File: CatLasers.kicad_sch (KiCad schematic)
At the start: 6 parts, among them J2 Programmer, J4 IR Emitter, J6 Conn_01x04, U2 ESP32-WROOM-32E_(4MB_HIGH_TEM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

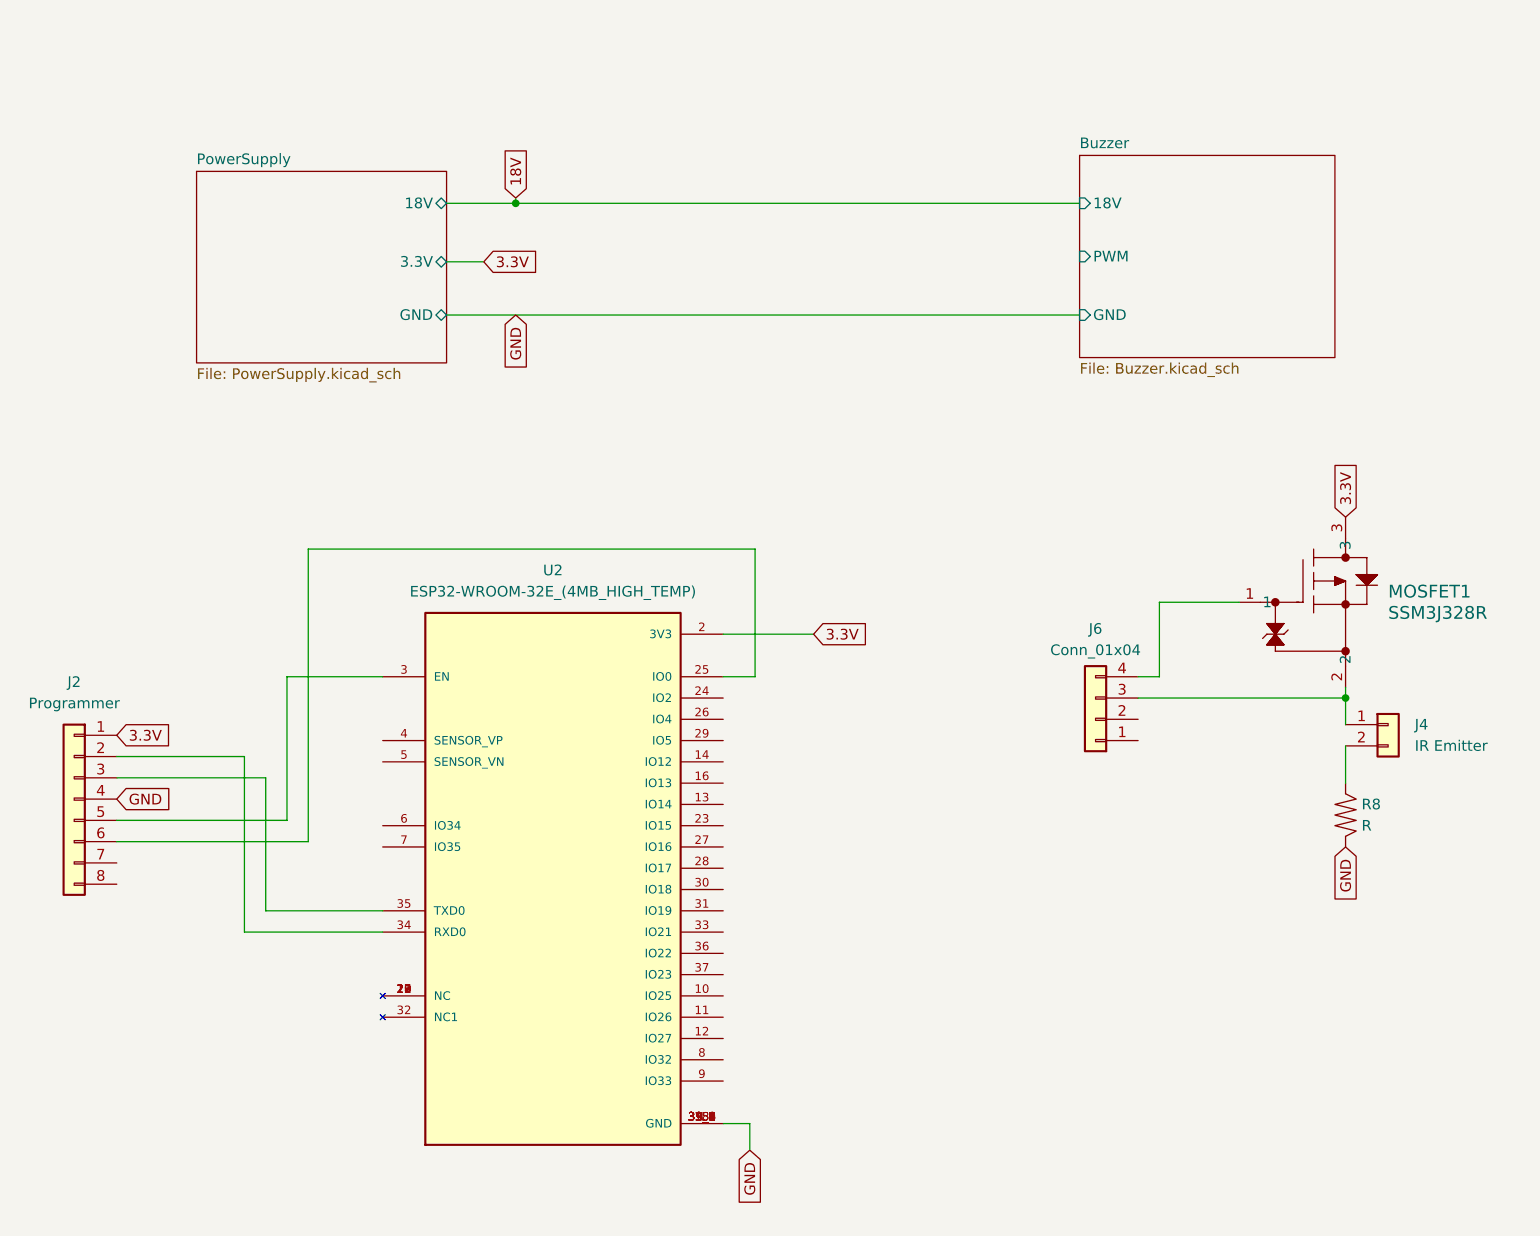
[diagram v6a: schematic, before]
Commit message: Wired MCU jumpers
All MCU pins are sent directly to jumpers. This will double as testpoints and a way for me to easily rewire the test board.
Footprints also assigned
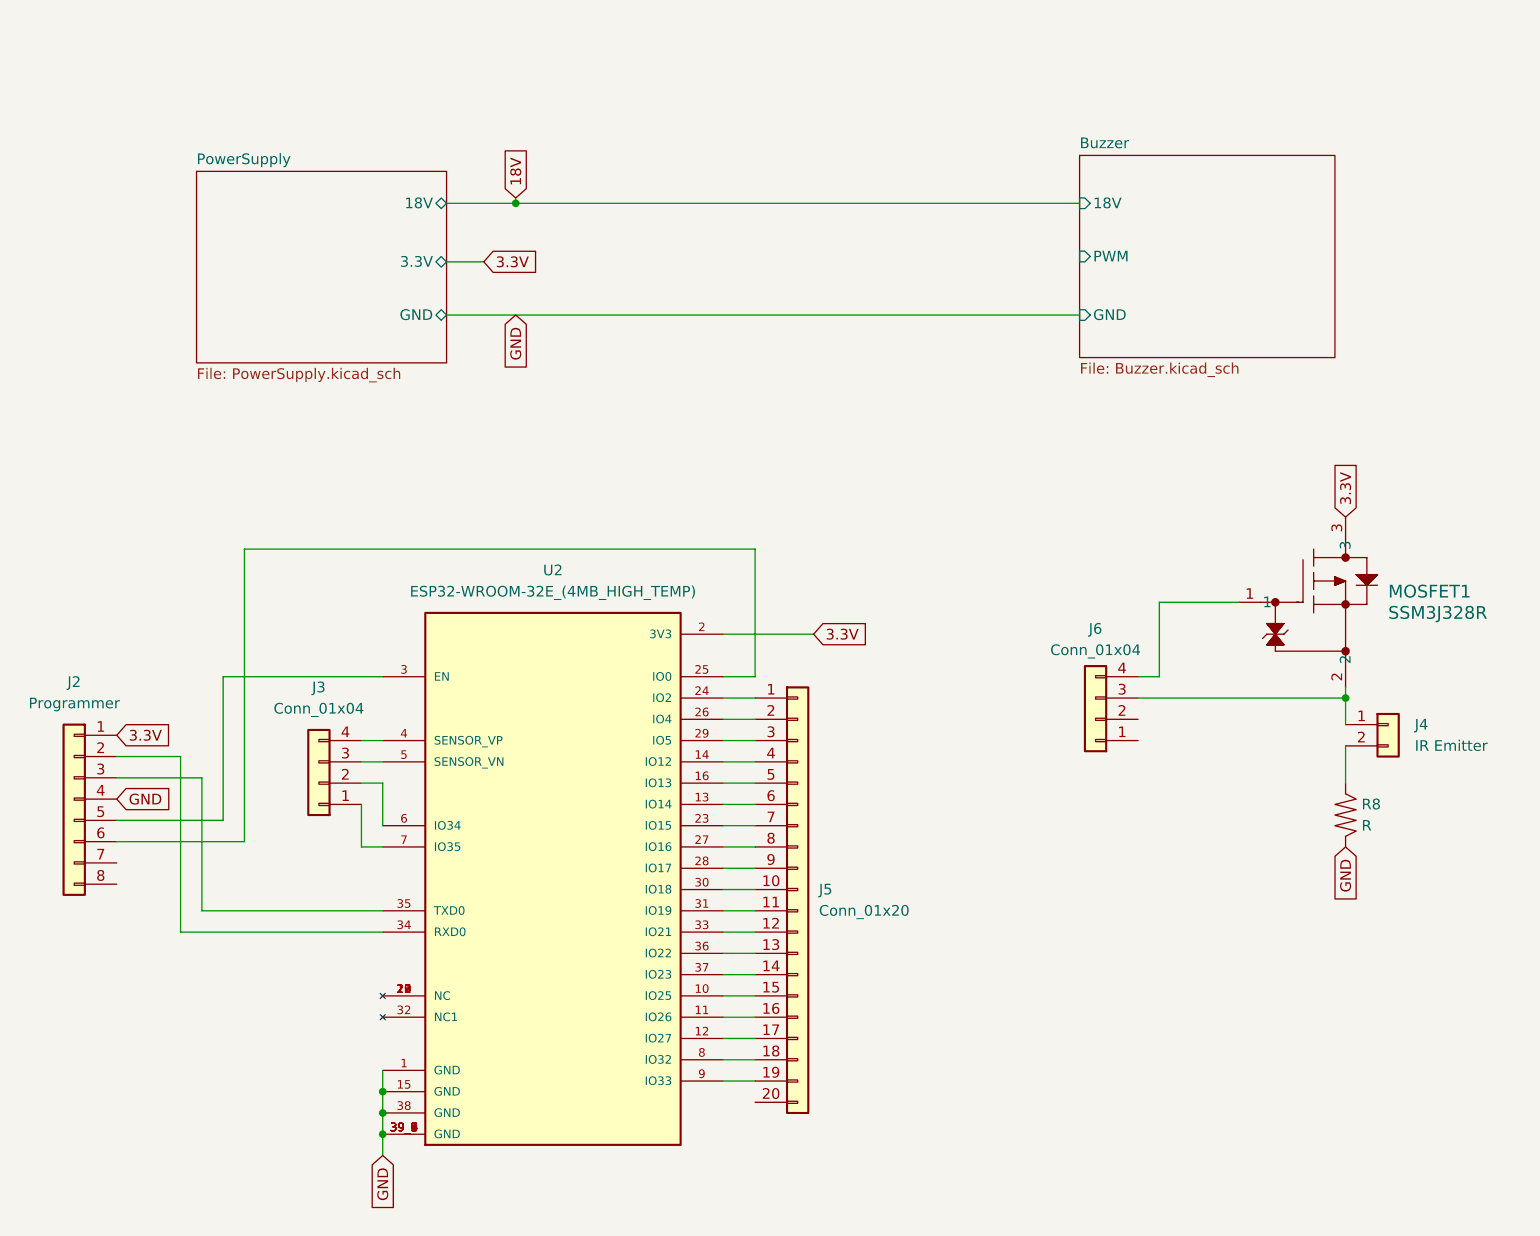
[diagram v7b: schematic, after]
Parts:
- added J3: Conn_01x04, Connector_PinHeader_2.54mm:PinHeader_1x04_P2.54mm_Vertical, symbol Connector_Generic:Conn_01x04
- added J5: Conn_01x20, Connector_PinHeader_2.54mm:PinHeader_1x20_P2.54mm_Vertical, symbol Connector_Generic:Conn_01x20
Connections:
- net at U2.10 (IO25): now also J5.15 (Pin_15)
- net at U2.11 (IO26): now also J5.16 (Pin_16)
- net at U2.12 (IO27): now also J5.17 (Pin_17)
- net at U2.13 (IO14): now also J5.6 (Pin_6)
- net at U2.14 (IO12): now also J5.4 (Pin_4)
- net at U2.16 (IO13): now also J5.5 (Pin_5)
- net at U2.23 (IO15): now also J5.7 (Pin_7)
- net at U2.24 (IO2): now also J5.1 (Pin_1)
- net at U2.26 (IO4): now also J5.2 (Pin_2)
- net at U2.27 (IO16): now also J5.8 (Pin_8)
- net at U2.28 (IO17): now also J5.9 (Pin_9)
- net at U2.29 (IO5): now also J5.3 (Pin_3)
- net at U2.30 (IO18): now also J5.10 (Pin_10)
- net at U2.31 (IO19): now also J5.11 (Pin_11)
- net at U2.33 (IO21): now also J5.12 (Pin_12)
- net at U2.36 (IO22): now also J5.13 (Pin_13)
- net at U2.37 (IO23): now also J5.14 (Pin_14)
- net at U2.4 (SENSOR_VP): now also J3.4 (Pin_4)
- net at U2.5 (SENSOR_VN): now also J3.3 (Pin_3)
- net at U2.6 (IO34): now also J3.2 (Pin_2)
- net at U2.7 (IO35): now also J3.1 (Pin_1)
- net at U2.8 (IO32): now also J5.18 (Pin_18)
- net at U2.9 (IO33): now also J5.19 (Pin_19)
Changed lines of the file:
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@@
   (junction (at 179.705 101.6) (diameter 0) (color 0 0 0 0)
   )
-  (wire (pts (xy 109.22 83.82) (xy 55.88 83.82))
-    (stroke (width 0) (type default))
-  )
-  (wire (pts (xy 50.8 111.125) (xy 33.02 111.125))
-    (stroke (width 0) (type default))
-  )
-  (wire (pts (xy 64.77 127) (xy 50.8 127))
+  (junction (at 64.77 153.67) (diameter 0) (color 0 0 0 0)
+  )
+  (junction (at 64.77 151.13) (diameter 0) (color 0 0 0 0)
+  )
+  (junction (at 64.77 148.59) (diameter 0) (color 0 0 0 0)
+  )
+  (wire (pts (xy 109.22 137.16) (xy 105.41 137.16))
+    (stroke (width 0) (type default))
+  )
+  (wire (pts (xy 109.22 83.82) (xy 48.26 83.82))
+    (stroke (width 0) (type default))
+  )
+  (wire (pts (xy 109.22 83.82) (xy 109.22 99.06))
+    (stroke (width 0) (type default))
+  )
+  (wire (pts (xy 109.22 144.78) (xy 105.41 144.78))
+    (stroke (width 0) (type default))
+  )
+  (wire (pts (xy 43.18 111.125) (xy 33.02 111.125))
+    (stroke (width 0) (type default))
+  )
+  (wire (pts (xy 64.77 127) (xy 43.18 127))
     (stroke (width 0) (type default))
   )
@@
     (stroke (width 0) (type default))
   )
-  (wire (pts (xy 50.8 127) (xy 50.8 111.125))
+  (wire (pts (xy 43.18 127) (xy 43.18 111.125))
     (stroke (width 0) (type default))
   )
@@
     (stroke (width 0) (type default))
   )
-  (wire (pts (xy 64.77 99.06) (xy 53.34 99.06))
+  (wire (pts (xy 64.77 99.06) (xy 45.72 99.06))
+    (stroke (width 0) (type default))
+  )
+  (wire (pts (xy 109.22 101.6) (xy 105.41 101.6))
     (stroke (width 0) (type default))
   )
@@
     (stroke (width 0) (type default))
   )
-  (wire (pts (xy 109.22 99.06) (xy 109.22 83.82))
-    (stroke (width 0) (type default))
-  )
-  (wire (pts (xy 48.26 129.54) (xy 48.26 108.585))
+  (wire (pts (xy 109.22 124.46) (xy 105.41 124.46))
+    (stroke (width 0) (type default))
+  )
+  (wire (pts (xy 109.22 139.7) (xy 105.41 139.7))
+    (stroke (width 0) (type default))
+  )
+  (wire (pts (xy 40.64 129.54) (xy 40.64 108.585))
+    (stroke (width 0) (type default))
+  )
+  (wire (pts (xy 64.77 119.38) (xy 62.23 119.38))
     (stroke (width 0) (type default))
   )
@@
     (stroke (width 0) (type default))
   )
-  (wire (pts (xy 53.34 99.06) (xy 53.34 116.205))
+  (wire (pts (xy 45.72 99.06) (xy 45.72 116.205))
+    (stroke (width 0) (type default))
+  )
+  (wire (pts (xy 109.22 132.08) (xy 105.41 132.08))
+    (stroke (width 0) (type default))
+  )
+  (wire (pts (xy 64.77 153.67) (xy 64.77 156.21))
     (stroke (width 0) (type default))
   )
@@
     (stroke (width 0) (type default))
   )
+  (wire (pts (xy 109.22 109.22) (xy 105.41 109.22))
+    (stroke (width 0) (type default))
+  )
+  (wire (pts (xy 109.22 129.54) (xy 105.41 129.54))
+    (stroke (width 0) (type default))
+  )
+  (wire (pts (xy 109.22 106.68) (xy 105.41 106.68))
+    (stroke (width 0) (type default))
+  )
   (wire (pts (xy 154.94 101.6) (xy 179.705 101.6))
     (stroke (width 0) (type default))
   )
-  (wire (pts (xy 53.34 116.205) (xy 33.02 116.205))
+  (wire (pts (xy 45.72 116.205) (xy 33.02 116.205))
+    (stroke (width 0) (type default))
+  )
+  (wire (pts (xy 64.77 148.59) (xy 64.77 151.13))
+    (stroke (width 0) (type default))
+  )
+  (wire (pts (xy 64.77 111.76) (xy 62.23 111.76))
+    (stroke (width 0) (type default))
+  )
+  (wire (pts (xy 64.77 146.05) (xy 64.77 148.59))
+    (stroke (width 0) (type default))
+  )
+  (wire (pts (xy 62.23 119.38) (xy 62.23 114.3))
+    (stroke (width 0) (type default))
+  )
+  (wire (pts (xy 64.77 116.84) (xy 64.77 111.76))
     (stroke (width 0) (type default))
   )
@@
     (stroke (width 0) (type default))
   )
+  (wire (pts (xy 109.22 134.62) (xy 105.41 134.62))
+    (stroke (width 0) (type default))
+  )
+  (wire (pts (xy 109.22 127) (xy 105.41 127))
+    (stroke (width 0) (type default))
+  )
+  (wire (pts (xy 109.22 121.92) (xy 105.41 121.92))
+    (stroke (width 0) (type default))
+  )
+  (wire (pts (xy 109.22 114.3) (xy 105.41 114.3))
+    (stroke (width 0) (type default))
+  )
+  (wire (pts (xy 109.22 119.38) (xy 105.41 119.38))
+    (stroke (width 0) (type default))
+  )
   (wire (pts (xy 157.48 99.06) (xy 157.48 90.17))
     (stroke (width 0) (type default))
   )
-  (wire (pts (xy 64.77 129.54) (xy 48.26 129.54))
+  (wire (pts (xy 64.77 129.54) (xy 40.64 129.54))
+    (stroke (width 0) (type default))
+  )
+  (wire (pts (xy 62.23 109.22) (xy 64.77 109.22))
     (stroke (width 0) (type default))
   )
@@
     (stroke (width 0) (type default))
   )
-  (wire (pts (xy 108.585 152.4) (xy 108.585 155.575))
-    (stroke (width 0) (type default))
-  )
-  (wire (pts (xy 55.88 118.745) (xy 33.02 118.745))
-    (stroke (width 0) (type default))
-  )
-  (wire (pts (xy 55.88 83.82) (xy 55.88 118.745))
+  (wire (pts (xy 48.26 118.745) (xy 33.02 118.745))
+    (stroke (width 0) (type default))
+  )
+  (wire (pts (xy 48.26 83.82) (xy 48.26 118.745))
     (stroke (width 0) (type default))
   )
@@
     (stroke (width 0) (type default))
   )
-  (wire (pts (xy 48.26 108.585) (xy 33.02 108.585))
+  (wire (pts (xy 109.22 111.76) (xy 105.41 111.76))
+    (stroke (width 0) (type default))
+  )
+  (wire (pts (xy 62.23 106.68) (xy 64.77 106.68))
+    (stroke (width 0) (type default))
+  )
+  (wire (pts (xy 109.22 116.84) (xy 105.41 116.84))
+    (stroke (width 0) (type default))
+  )
+  (wire (pts (xy 109.22 142.24) (xy 105.41 142.24))
+    (stroke (width 0) (type default))
+  )
+  (wire (pts (xy 109.22 147.32) (xy 105.41 147.32))
+    (stroke (width 0) (type default))
+  )
+  (wire (pts (xy 40.64 108.585) (xy 33.02 108.585))
     (stroke (width 0) (type default))
   )
@@
     (stroke (width 0) (type default))
   )
-  (wire (pts (xy 105.41 152.4) (xy 108.585 152.4))
+  (wire (pts (xy 109.22 104.14) (xy 105.41 104.14))
+    (stroke (width 0) (type default))
+  )
+  (wire (pts (xy 64.77 151.13) (xy 64.77 153.67))
     (stroke (width 0) (type default))
   )
@@
     )
   )
-  (global_label "GND" (shape input) (at 108.585 155.575 270) (fields_autoplaced)
+  (global_label "GND" (shape input) (at 64.77 156.21 270) (fields_autoplaced)
     (effects (font (size 1.27 1.27)) (justify right))
-    (property "Intersheetrefs" "${INTERSHEET_REFS}" (at 108.585 162.4307 90)
+    (property "Intersheetrefs" "${INTERSHEET_REFS}" (at 64.77 163.0657 90)
       (effects (font (size 1.27 1.27)) (justify right) hide)
     )
@@
     (property "Intersheetrefs" "${INTERSHEET_REFS}" (at 83.9326 49.53 0)
       (effects (font (size 1.27 1.27)) (justify left) hide)
+    )
+  )
+  (symbol (lib_id "Connector_Generic:Conn_01x20") (at 114.3 124.46 0) (unit 1)
+    (in_bom yes) (on_board yes) (dnp no) (fields_autoplaced)
+    (property "Reference" "J5" (at 116.84 124.46 0)
+      (effects (font (size 1.27 1.27)) (justify left))
+    )
+    (property "Value" "Conn_01x20" (at 116.84 127 0)
+      (effects (font (size 1.27 1.27)) (justify left))
+    )
+    (property "Footprint" "Connector_PinHeader_2.54mm:PinHeader_1x20_P2.54mm_Vertical" (at 114.3 124.46 0)
+      (effects (font (size 1.27 1.27)) hide)
+    )
+    (property "Datasheet" "~" (at 114.3 124.46 0)
+      (effects (font (size 1.27 1.27)) hide)
+    )
+    (pin "1")
+    (pin "10")
+    (pin "11")
+    (pin "12")
+    (pin "13")
+    (pin "14")
+    (pin "15")
+    (pin "16")
+    (pin "17")
+    (pin "18")
+    (pin "19")
+    (pin "2")
+    (pin "20")
+    (pin "3")
+    (pin "4")
+    (pin "5")
+    (pin "6")
+    (pin "7")
+    (pin "8")
+    (pin "9")
+    (instances
+      (project "CatLasers"
+        (path "/b94f5b10-ee0c-4425-b025-e3a8bb3cc7b0"
+          (reference "J5") (unit 1)
+        )
+      )
     )
   )
@@
         )
       )
+    )
+  )
+  (symbol (lib_id "Connector_Generic:Conn_01x04") (at 57.15 111.76 180) (unit 1)
+    (in_bom yes) (on_board yes) (dnp no) (fields_autoplaced)
+    (property "Reference" "J3" (at 57.15 100.33 0)
+      (effects (font (size 1.27 1.27)))
+    )
+    (property "Value" "Conn_01x04" (at 57.15 102.87 0)
+      (effects (font (size 1.27 1.27)))
+    )
+    (property "Footprint" "Connector_PinHeader_2.54mm:PinHeader_1x04_P2.54mm_Vertical" (at 57.15 111.76 0)
+      (effects (font (size 1.27 1.27)) hide)
+    )
+    (property "Datasheet" "~" (at 57.15 111.76 0)
+      (effects (font (size 1.27 1.27)) hide)
+    )
+    (pin "1")
+    (pin "2")
+    (pin "3")
+    (pin "4")
+    (instances
+      (project "CatLasers"
+        (path "/b94f5b10-ee0c-4425-b025-e3a8bb3cc7b0"
+          (reference "J3") (unit 1)
+        )
+      )
